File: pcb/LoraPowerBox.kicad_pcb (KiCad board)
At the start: 4 copper layers, 51.6 x 61.1 mm, 48 parts, among them J1 Conn_01x04_Pin, J10 Conn_01x02_Pin, J11 Conn_01x02_Pin, J12 Conn_01x05_Pin, J2 Conn_01x04_Pin, J3 Conn_01x04_Pin, J4 Conn_01x06_Pin, J5 Conn_01x04_Pin, J6 Conn_01x04_Pin, J7 Conn_01x04_Pin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

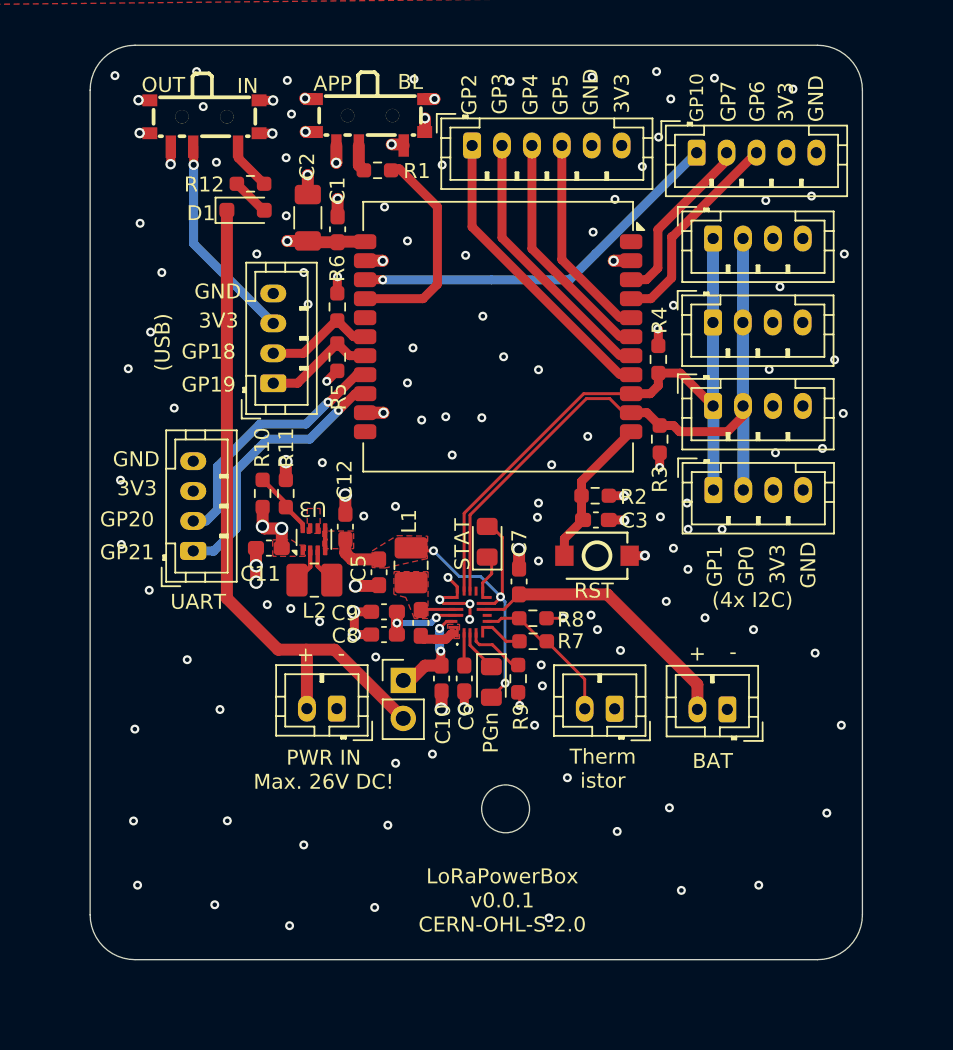
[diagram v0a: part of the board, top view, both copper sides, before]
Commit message: pcb: reduce edge cut size a bit
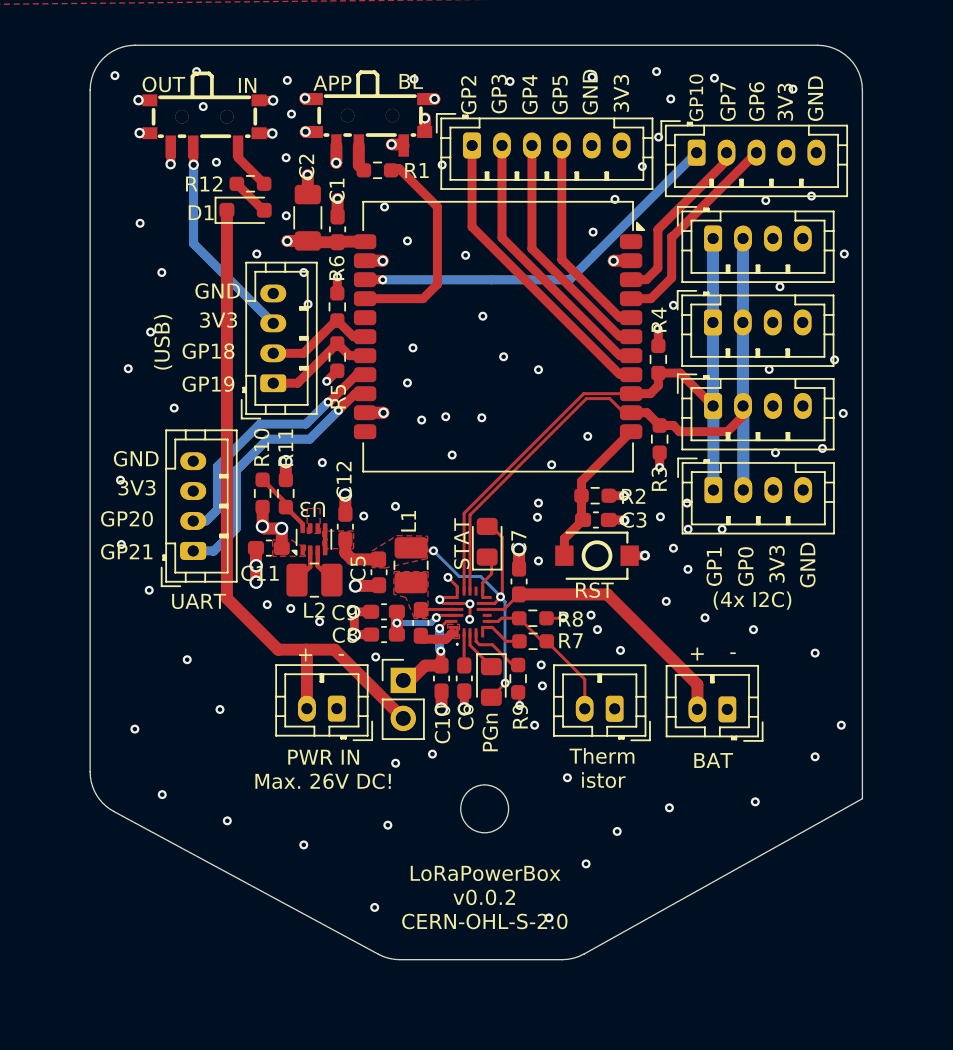
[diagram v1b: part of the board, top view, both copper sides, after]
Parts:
- moved H1 1.40 mm to (138.3, 90.4)
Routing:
- net GND: vias 134 -> 131
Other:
- outline, holes or cut-outs redrawn
- board text added: "LoRaPowerBox v0.0.2 CERN-OHL-S-2.0"
- board text removed: "LoRaPowerBox v0.0.1 CERN-OHL-S-2.0"
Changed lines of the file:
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@@
 		(13 "F.Paste" user)
 		(15 "B.Paste" user)
-		(5 "F.SilkS" user)
-		(7 "B.SilkS" user)
+		(5 "F.SilkS" user "F.Silkscreen")
+		(7 "B.SilkS" user "B.Silkscreen")
 		(1 "F.Mask" user)
 		(3 "B.Mask" user)
 		(25 "Edge.Cuts" user)
 		(27 "Margin" user)
-		(31 "F.CrtYd" user)
-		(29 "B.CrtYd" user)
+		(31 "F.CrtYd" user "F.Courtyard")
+		(29 "B.CrtYd" user "B.Courtyard")
 		(35 "F.Fab" user)
 	)
@@
 	(footprint "MountingHole:MountingHole_3.2mm_M3"
 		(layer "F.Cu")
-		(at 139.71 90.42)
+		(at 138.31 90.42)
 		(descr "Mounting Hole 3.2mm, M3, no annular, generated by kicad-footprint-generator mountinghole.py")
 		(tags "mountinghole M3")
@@
 	)
 	(gr_arc
-		(start 163.56 97.5)
-		(mid 162.68132 99.62132)
-		(end 160.56 100.5)
-		(stroke
-			(width 0.05)
-			(type default)
-		)
-		(layer "Edge.Cuts")
-	)
-	(gr_arc
-		(start 114.94 100.5)
-		(mid 112.81868 99.62132)
-		(end 111.94 97.5)
+		(start 144.961525 100.119647)
+		(mid 144.254858 100.40336)
+		(end 143.499523 100.5)
 		(stroke
 			(width 0.05)
@@
 	)
 	(gr_line
-		(start 163.56 97.5)
+		(start 163.56 89.74)
 		(end 163.56 42.38)
 		(stroke
@@
 	)
 	(gr_line
+		(start 144.961525 100.119647)
+		(end 163.56 89.74)
+		(stroke
+			(width 0.0381)
+			(type default)
+		)
+		(layer "Edge.Cuts")
+	)
+	(gr_line
 		(start 111.94 42.38)
-		(end 111.94 97.5)
+		(end 111.94 87.949942)
+		(stroke
+			(width 0.05)
+			(type default)
+		)
+		(layer "Edge.Cuts")
+	)
+	(gr_arc
+		(start 132.637784 100.5)
+		(mid 131.903077 100.408643)
+		(end 131.213116 100.140137)
 		(stroke
 			(width 0.05)
@@
 	)
 	(gr_line
-		(start 114.94 100.5)
-		(end 160.56 100.5)
+		(start 132.637784 100.5)
+		(end 143.499523 100.5)
 		(stroke
 			(width 0.05)
@@
 		(layer "Edge.Cuts")
 	)
+	(gr_arc
+		(start 113.515332 90.590079)
+		(mid 112.363746 89.48715)
+		(end 111.94 87.949942)
+		(stroke
+			(width 0.05)
+			(type default)
+		)
+		(layer "Edge.Cuts")
+	)
+	(gr_line
+		(start 113.515332 90.590079)
+		(end 131.213116 100.140137)
+		(stroke
+			(width 0.0381)
+			(type default)
+		)
+		(layer "Edge.Cuts")
+	)
 	(gr_text "-"
 		(at 155.16 79.52 180)
@@
 		)
 	)
-	(gr_text "LoRaPowerBox\nv0.0.1\nCERN-OHL-S-2.0\n"
-		(at 139.49 98.74 0)
+	(gr_text "LoRaPowerBox\nv0.0.2\nCERN-OHL-S-2.0\n"
+		(at 138.33 98.57 0)
 		(layer "F.SilkS")
 		(effects
@@
 	)
 	(via
-		(at 161.18 90.7)
+		(at 160.4 86.94)
 		(size 0.6)
 		(drill 0.3)
@@
 	)
 	(via
-		(at 120.27 96.83)
-		(size 0.6)
-		(drill 0.3)
-		(layers "F.Cu" "B.Cu")
-		(free yes)
-		(net 1)
-	)
-	(via
 		(at 146.93 53.79)
 		(size 0.7)
@@
 	)
 	(via
-		(at 151.46 95.87)
+		(at 145.09 94.1)
 		(size 0.6)
 		(drill 0.3)
@@
 	)
 	(via
-		(at 125.27 98.23)
-		(size 0.6)
-		(drill 0.3)
-		(layers "F.Cu" "B.Cu")
-		(free yes)
-		(net 1)
-	)
-	(via
 		(at 131.62 50.19)
 		(size 0.6)
@@
 	)
 	(via
-		(at 114.84 91.23)
+		(at 116.76 89.47)
 		(size 0.6)
 		(drill 0.3)
@@
 	)
 	(via
-		(at 115.11 95.52)
-		(size 0.6)
-		(drill 0.3)
-		(layers "F.Cu" "B.Cu")
-		(free yes)
-		(net 1)
-	)
-	(via
 		(at 157.33 61.05)
 		(size 0.6)
@@
 	)
 	(via
-		(at 156.63 95.52)
+		(at 156.4 89.95)
 		(size 0.6)
 		(drill 0.3)
